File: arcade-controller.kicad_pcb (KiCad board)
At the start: 2 copper layers, 10 parts, among them J1 Conn_01x05_Pin, SW1 SW_Push, SW2 SW_Push, SW3 SW_Push, SW4 SW_Push, SW5 SW_Push, SW6 SW_Push, SW7 SW_Push, SW8 SW_Push

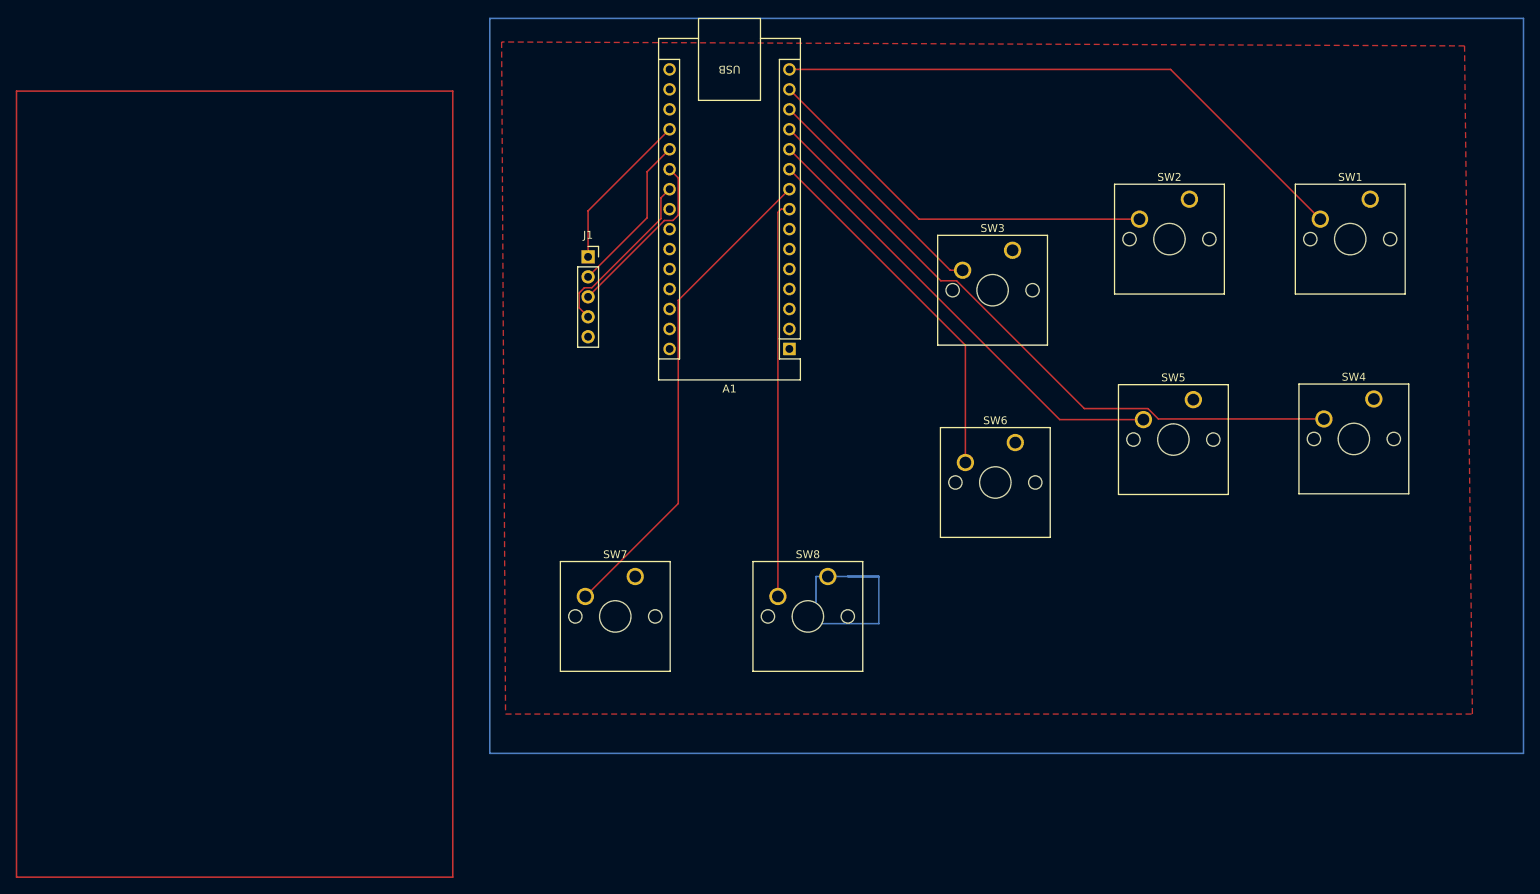
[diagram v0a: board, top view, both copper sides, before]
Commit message: Fixed it with proMicro
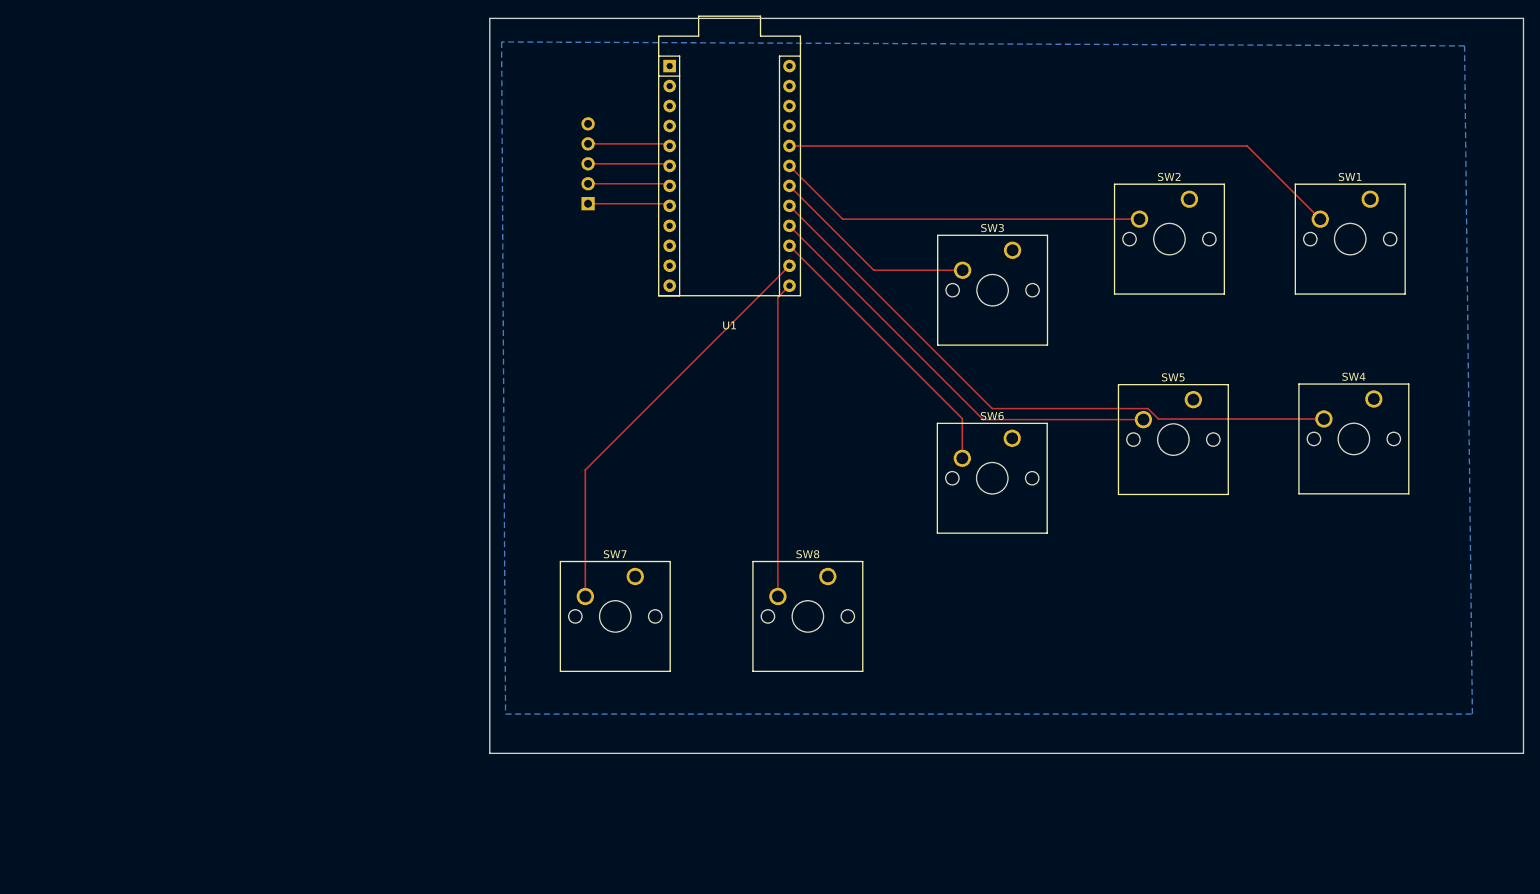
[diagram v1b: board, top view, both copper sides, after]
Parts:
- removed A1: Arduino_Nano_v3.x, Module:Arduino_Nano
- added U1: Sparkfun_Pro_Micro, ArcadeController:Sparkfun_Pro_Micro, F.Cu at (138.1, 69.0)
- J1: moved to B.Cu
- moved J1 6.76 mm to (112.5, 58.6)
- moved SW6 0.67 mm to (166.5, 88.4)
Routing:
- net Net-(J1-Pin_3): track 22.1 -> 10.5 mm
- net Net-(J1-Pin_4): track 22.0 -> 10.5 mm
- net Net-(U1-D14): track 46.6 -> 36.1 mm
- net Net-(U1-~D10/A10): track 50.5 -> 40.1 mm
- net Net-(J1-Pin_1): track 20.5 -> 10.5 mm
- net Net-(J1-Pin_2): track 20.5 -> 10.5 mm
- net Net-(U1-D16): track 62.6 -> 52.8 mm
- net Net-(U1-D19/A1): track 30.5 -> 26.5 mm
- net Net-(U1-D15): track 59.3 -> 55.2 mm
- net Net-(U1-D21/A3): track 75.4 -> 71.4 mm
- net Net-(U1-D20/A2): track 51.4 -> 47.3 mm
- net Net-(U1-D18/A0): track 83.3 -> 79.2 mm
- added copper zone on B.Cu, net GND
- removed copper zone on F.Cu, net GND
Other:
- board outline added: 131.5 x 93.5 mm
- board text removed: "Sanwa Joystick"

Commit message: test 1
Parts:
- removed SW3: SW_Push, Button_Switch_Keyboard:SW_Cherry_MX_1.00u_PCB

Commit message: undo test
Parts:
- added SW3: SW_Push, Button_Switch_Keyboard:SW_Cherry_MX_1.00u_PCB, F.Cu at (166.5, 64.5)

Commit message: added mounting holes
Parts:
- added H1: MountingHole, MountingHole:MountingHole_3.2mm_M3, F.Cu at (219.5, 118.7)
- added H2: MountingHole, MountingHole:MountingHole_3.2mm_M3, F.Cu at (99.0, 118.7)
- added H3: MountingHole, MountingHole:MountingHole_3.2mm_M3, F.Cu at (99.0, 43.5)
- added H4: MountingHole, MountingHole:MountingHole_3.2mm_M3, F.Cu at (219.5, 43.5)
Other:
- board size 131.5 x 93.5 mm -> 141.5 x 93.5 mm

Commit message: Generated gerber files, submitted for class
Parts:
- J1: moved to F.Cu
- turned J1 to 180 degrees
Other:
- board size 141.5 x 93.5 mm -> 137.5 x 93.5 mm
